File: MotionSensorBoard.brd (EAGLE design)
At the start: 69.8 x 69.5 mm, 26 parts, among them J1 PRGM, J2 POWER_JACKPTH, U1 ATTINY2313A-SUR, U2 ISO7221ADR, U4 NCP1117ST50T3G, U5 LM1117MPX-3.3

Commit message: updated schematic
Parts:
- removed C5: 0.1uF, SparkFun-Passives:0603-CAP
- removed C8: 10uF, Passives:PANASONIC_BMIN
- removed JP2: (no value), SparkFun-Connectors:1X07
- removed S1: SWITCH, SparkFun-Electromechanical:TACTILE-PTH
- removed Y2: (no value), SparkFun-FreqCtrl:RESONATOR-PTH
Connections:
- removed net N$1: U1.4, Y2.1
- removed net N$2: U1.5, Y2.3
- removed net N$3: JP2.7, U1.16
- removed net N$4: JP2.6, U1.15
- removed net N$5: JP2.5, U1.14
- removed net N$6: JP2.4, U1.13
- net 3.3V: no longer JP2.2
- net GND: now also JP1.1; no longer C5.2, C8.-, JP1.3, JP2.1, S1.1, Y2.2
- net RESET: no longer C5.1, S1.3
- net SIGIN: now also JP1.3; no longer JP1.1, JP2.3
- net VIN: no longer C8.+
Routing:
- net N$3: track 33.8 -> 0.00 mm
- net N$4: track 29.1 -> 0.00 mm
- net N$5: track 24.0 -> 0.00 mm
- net SIGIN: track 55.5 -> 33.9 mm
- net N$6: track 18.9 -> 0.00 mm
- net N$1: track 12.5 -> 0.00 mm
- net N$2: track 8.38 -> 0.00 mm
- net VIN: track 44.2 -> 38.6 mm
- net RESET: track 65.3 -> 62.2 mm
- net 3.3V: track 71.5 -> 70.3 mm

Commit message: Schematic Updated
Schematic Rev A major revisions complete
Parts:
- removed U1: ATTINY2313A-SUR, microcontrollers-atmel:20S
- added JP4: M02PTH, SparkFun-Connectors:1X02
- added Q1, Q2: BSS138, SparkFun-DiscreteSemi:SOT23
- added R2, R3, R6, R7: 4.7k, SparkFun-Resistors:0603-RES
- added R4: PHOTOCELLPTH, SparkFun-Sensors:PHOTOCELL
- added R5: 10k, SparkFun-Resistors:0603-RES
- added U3: BMP180, SparkFun-Sensors:BMP180
- added U6: HTU21DSMD, SparkFun-Sensors:HTU21D
- added U7: ATMEGA328P, SparkFun-DigitalIC:TQFP32-08
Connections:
- new net LHT: R4.1, R5.2, U7.23
- new net SCL_3_3V: Q2.2, R2.1, U3.5, U6.SCK
- new net SCL_5V: Q2.3, R6.1, U7.28
- new net SDA_3_3V: Q1.2, R3.1, U3.6, U6.DATA
- new net SDA_5V: Q1.3, R7.1, U7.27
- net 3.3V: now also Q1.1, Q2.1, R2.2, R3.2, U3.2, U3.3, U6.VDD
- net 5V: now also R4.2, R6.2, R7.2, U7.18, U7.4, U7.6; no longer U1.20
- net GND: now also JP4.1, R5.1, U3.7, U6.7, U6.GND, U7.21, U7.3, U7.5; no longer U1.10
- net MISO: now also U7.16; no longer U1.18
- net MOSI: now also U7.15; no longer U1.17
- net RESET: now also U7.29; no longer U1.1
- net RXD: now also U7.30; no longer U1.2
- net SCK: now also U7.17; no longer U1.19
- net SIGIN: now also U7.9; no longer U1.12
- net TXD: now also U7.31; no longer U1.3
- net VIN: now also JP4.2
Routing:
- net SIGIN: track 33.9 -> 0.00 mm
- net RXD: track 16.4 -> 8.18 mm
- net 5V: track 107.5 -> 101.8 mm
- net RESET: track 62.2 -> 57.8 mm
- net MISO: track 28.8 -> 25.6 mm
- net MOSI: track 27.8 -> 24.6 mm
- net TXD: track 12.4 -> 10.5 mm
- net SCK: track 41.2 -> 39.3 mm

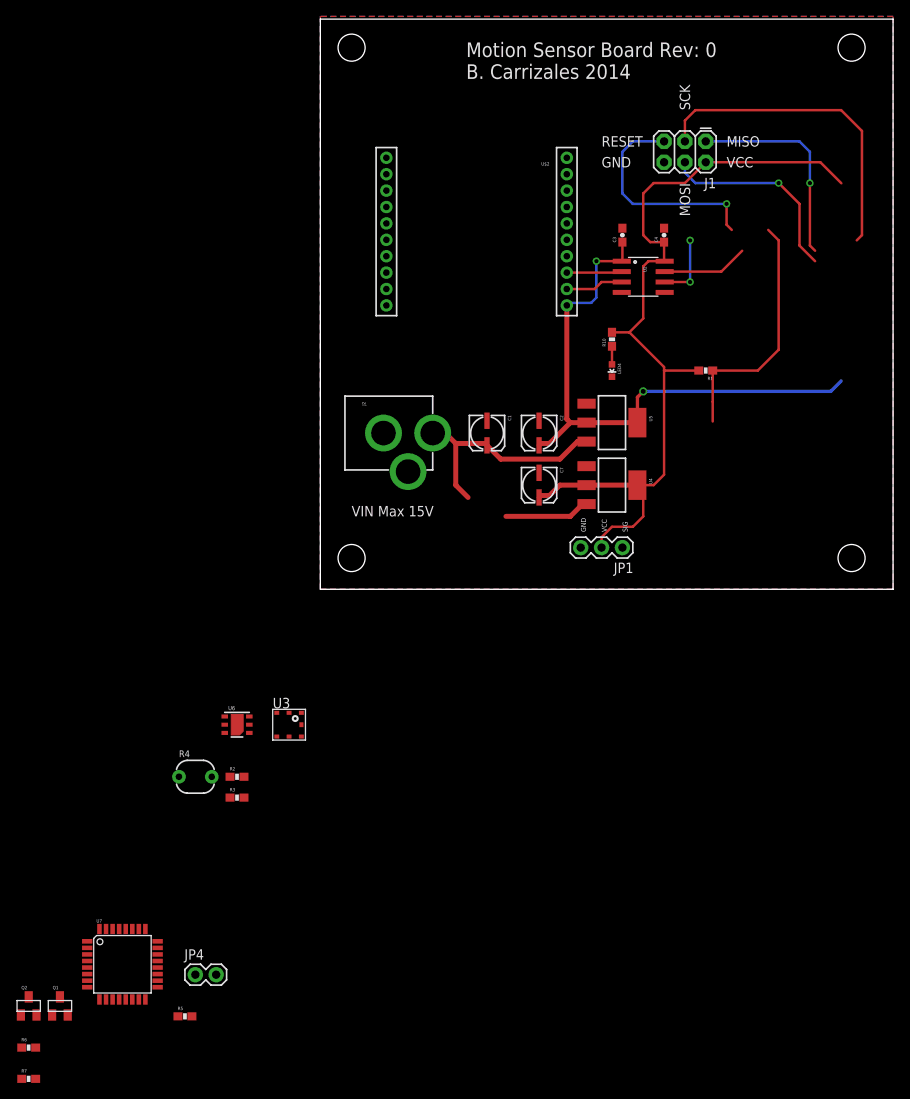
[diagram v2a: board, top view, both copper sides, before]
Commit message: updated board layout and generated Gerbers
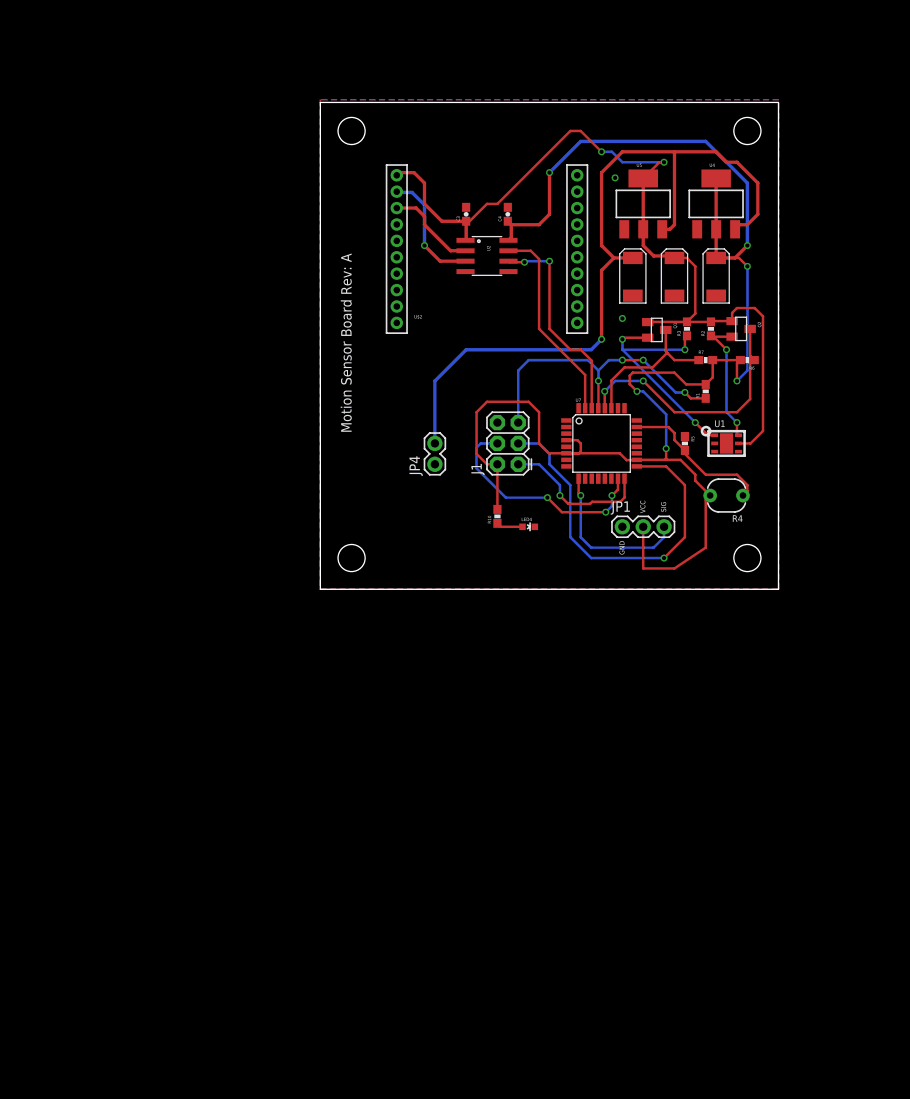
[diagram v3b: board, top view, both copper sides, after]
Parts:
- removed C7: 10uF, Passives:PANASONIC_BMIN
- removed J2: POWER_JACKPTH, SparkFun-Connectors:POWER_JACK_PTH
- removed U3: BMP180, SparkFun-Sensors:BMP180
- removed U6: HTU21DSMD, SparkFun-Sensors:HTU21D
- added C5: 10uF, SparkFun-Passives:EIA6032
- added U1: SI7006DFN6, DigitalICs:DFN-6
- C1, C2: device Passives:PANASONIC_BMIN -> SparkFun-Passives:EIA6032
- moved R6 121.3 mm to (52.1, 27.9), turned to 180 degrees
- moved R7 120.4 mm to (47.0, 27.9)
- moved Q2 119.8 mm to (51.3, 31.8), turned to 270 degrees
- moved Q1 110.0 mm to (41.0, 31.6), turned to 270 degrees
- moved R5 92.7 mm to (44.5, 17.8), turned to 270 degrees
- moved U7 86.3 mm to (34.3, 17.8)
- moved STANDOFF2 80.2 mm to (3.81, 55.9)
- moved R2 79.5 mm to (47.6, 31.8), turned to 90 degrees
- moved R3 79.2 mm to (44.7, 31.8), turned to 90 degrees
- moved R4 73.3 mm to (49.5, 11.4), turned to 180 degrees
- moved STANDOFF1 71.0 mm to (52.1, 55.9)
- moved JP4 68.7 mm to (14.0, 15.2), turned to 90 degrees
- moved STANDOFF3 63.5 mm to (52.1, 3.81)
- moved STANDOFF4 62.2 mm to (3.81, 3.81)
- moved J1 45.5 mm to (24.1, 15.2), turned to 90 degrees
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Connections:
- net 3.3V: now also C2.P$1, U1.5; no longer C2.+, U3.2, U3.3, U6.VDD
- net 5V: now also C5.P$1; no longer C7.+
- net GND: now also C1.P$2, C2.P$2, C5.P$2, U1.2; no longer C1.-, C2.-, C7.-, J2.GND, J2.GNDBREAK, U3.7, U6.7, U6.GND
- net SCL_3_3V: now also U1.6; no longer U3.5, U6.SCK
- net SDA_3_3V: now also U1.1; no longer U3.6, U6.DATA
- net VIN: now also C1.P$1; no longer C1.+, J2.PWR
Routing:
- net 5V: track 101.8 -> 188.2 mm, vias 0 -> 6
- net VIN: track 38.6 -> 93.6 mm, vias 0 -> 1
- net 3.3V: track 70.3 -> 106.7 mm
- net SCL_5V: track 0.00 -> 31.8 mm, vias 0 -> 2
- net SDA_3_3V: track 0.00 -> 29.4 mm, vias 0 -> 3
- net RESET: track 57.8 -> 37.3 mm, vias 1 -> 4
- net SIGIN: track 0.00 -> 19.7 mm, vias 0 -> 1
- net SDA_5V: track 0.00 -> 18.7 mm
- net LHT: track 0.00 -> 18.7 mm
- net RXD: track 8.18 -> 25.9 mm
- net SCL_3_3V: track 0.00 -> 15.9 mm, vias 0 -> 2
- net TXD: track 10.5 -> 24.7 mm
- net DOUT: track 7.06 -> 14.8 mm, vias 0 -> 1
- net MISO: track 25.6 -> 18.3 mm
- net SCK: track 39.3 -> 44.8 mm, vias 0 -> 1
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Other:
- board size 69.8 x 69.5 mm -> 55.9 x 59.4 mm
- board text added: "Motion Sensor Board Rev: A"
- board text removed: "MISO"
- board text removed: "MOSI"
- board text removed: "Motion Sensor Board Rev: 0 B. Carrizales 2014"
- board text removed: "RESET"
- board text removed: "SCK"
- board text removed: "VIN Max 15V"
